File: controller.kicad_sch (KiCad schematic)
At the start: 40 parts, among them IC10 NXB0108BQX, IC11 STM32L475RGT6, IC12 W25N512GVEIG, J1 20021121-00014T4LF, J2 10118192-0001LF, Y3 ECS-.327-7-1210-TR

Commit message: Add company name (using github URL), date, and change revision number to all schematic pages
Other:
- company: (none) -> github.com/fuad1502/open-running-watch-hw
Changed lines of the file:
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@@
 	(title_block
 		(title "Open Running Watch")
-		(rev "A")
+		(date "2024-04-12")
+		(rev "0.1.0")
+		(company "github.com/fuad1502/open-running-watch-hw")
 	)
 	(junction

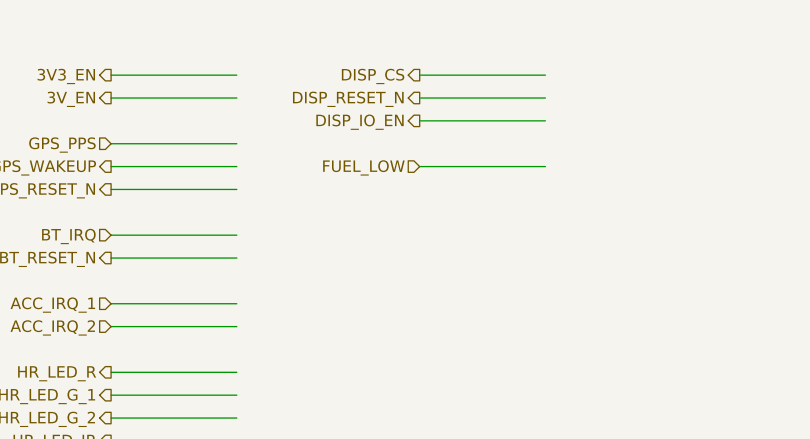
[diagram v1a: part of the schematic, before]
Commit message: Changed display to 12616-06 Sharp MIP display with Azumo backlight
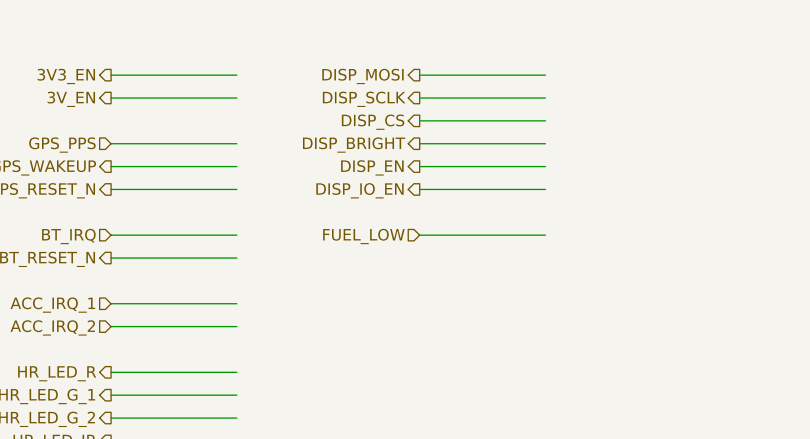
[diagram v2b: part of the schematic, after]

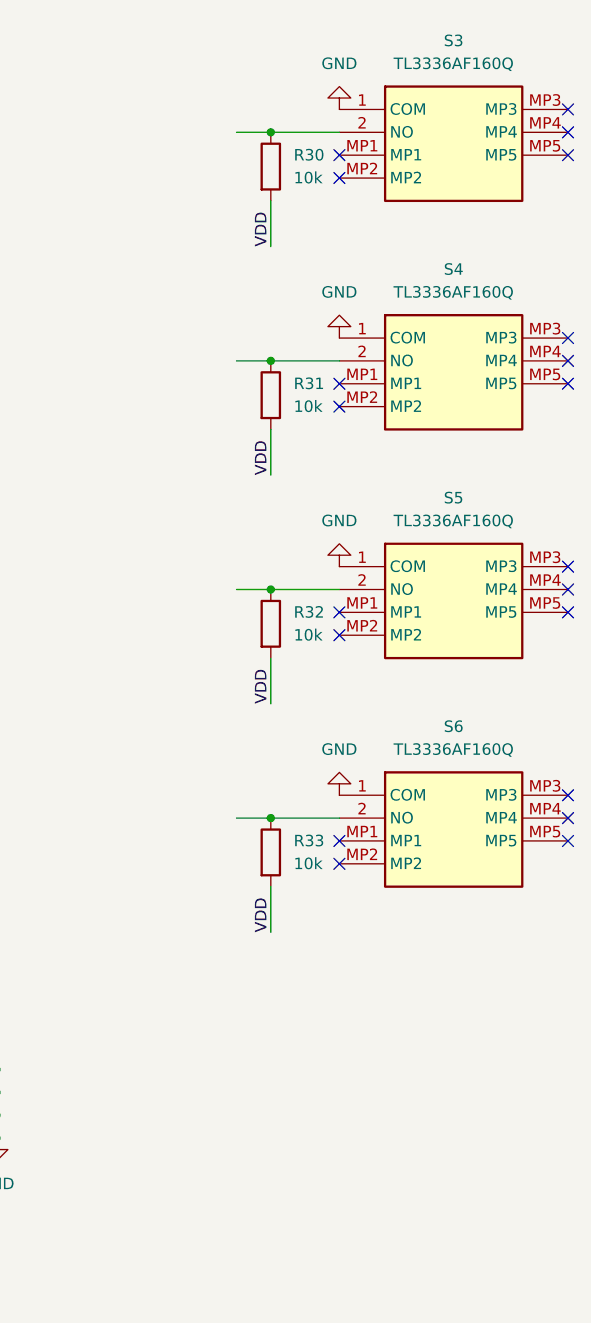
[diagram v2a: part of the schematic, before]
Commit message: Changed to smaller tactile switch
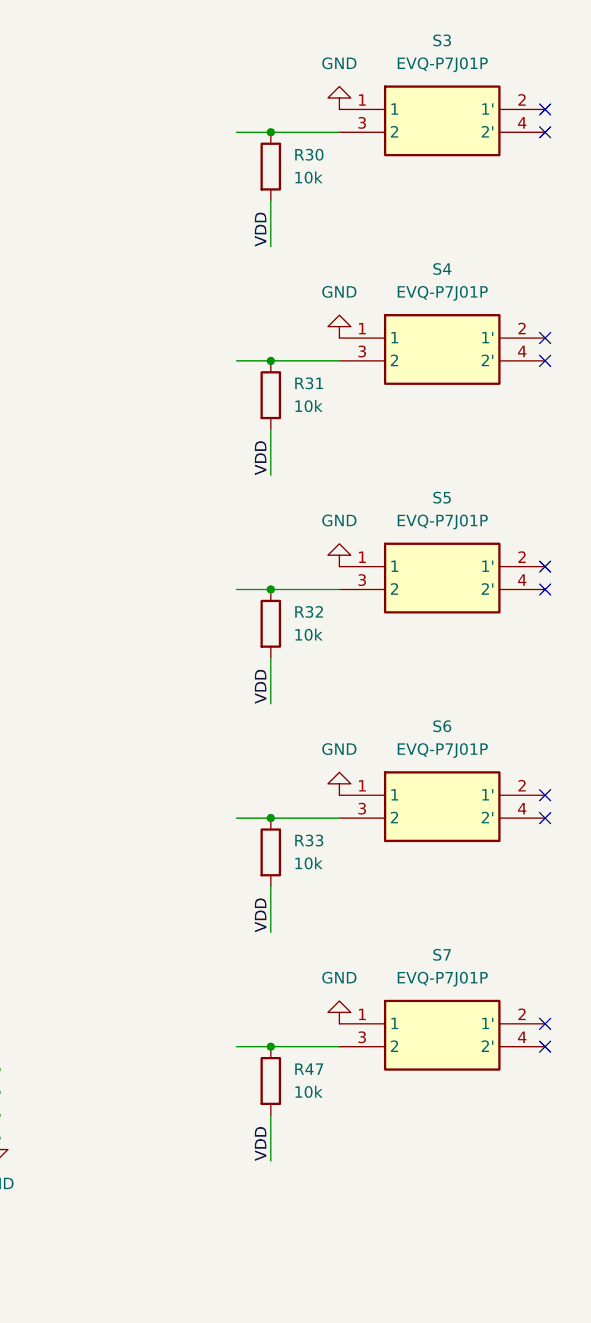
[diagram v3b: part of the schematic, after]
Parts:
- removed S3, S4, S5, S6: TL3336AF160Q, TL3336AF160Q:TL3336AF160Q, symbol TL3336AF160Q:TL3336AF160Q
- added R47: 10k, Resistor_SMD:R_0402_1005Metric_Pad0.72x0.64mm_HandSolder, symbol Device:R
- added S3, S4, S5, S6, S7: EVQ-P7J01P, EVQ-P7J01P:EVQP7J01P, symbol EVQ-P7J01P:EVQ-P7J01P
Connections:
- net GND: now also S3.1, S4.1, S5.1, S6.1, S7.1
- net VDD: now also R47.2
- net at R33.1: now also S6.3 (2)
- net at R32.1: now also S5.3 (2)
- net at R30.1: now also S3.3 (2)
- net at R31.1: now also S4.3 (2)
- new net: R47.1, S7.3 (2)
- no-connect marks 45 -> 35

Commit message: Changed hand soldered footprints to normal footprints
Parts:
- C43, C44, C45, C46, C51, C52, C53, C54, C55, C61, C62: footprint Capacitor_SMD:C_0402_1005Metric_Pad0.74x0.62mm_HandSolder -> Capacitor_SMD:C_0402_1005Metric
- C47, C48, C49, C50, C56, C57, C58, C59, C60: footprint Capacitor_SMD:C_0603_1608Metric_Pad1.08x0.95mm_HandSolder -> Capacitor_SMD:C_0603_1608Metric
- R26, R27, R28, R29, R30, R31, R32, R33, R47: footprint Resistor_SMD:R_0402_1005Metric_Pad0.72x0.64mm_HandSolder -> Resistor_SMD:R_0402_1005Metric
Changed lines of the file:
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@@
 			)
 		)
-		(property "Footprint" "Capacitor_SMD:C_0603_1608Metric_Pad1.08x0.95mm_HandSolder"
+		(property "Footprint" "Capacitor_SMD:C_0603_1608Metric"
 			(at 51.7652 231.14 0)
 			(effects
@@
 			)
 		)
-		(property "Footprint" "Capacitor_SMD:C_0402_1005Metric_Pad0.74x0.62mm_HandSolder"
+		(property "Footprint" "Capacitor_SMD:C_0402_1005Metric"
 			(at 64.4652 208.28 0)
 			(effects
@@
 			)
 		)
-		(property "Footprint" "Capacitor_SMD:C_0402_1005Metric_Pad0.74x0.62mm_HandSolder"
+		(property "Footprint" "Capacitor_SMD:C_0402_1005Metric"
 			(at 140.6652 166.37 0)
 			(effects
@@
 			)
 		)
-		(property "Footprint" "Capacitor_SMD:C_0603_1608Metric_Pad1.08x0.95mm_HandSolder"
+		(property "Footprint" "Capacitor_SMD:C_0603_1608Metric"
 			(at 77.1652 208.28 0)
 			(effects
@@
 			)
 		)
-		(property "Footprint" "Capacitor_SMD:C_0402_1005Metric_Pad0.74x0.62mm_HandSolder"
+		(property "Footprint" "Capacitor_SMD:C_0402_1005Metric"
 			(at 64.4652 182.88 0)
 			(effects
@@
 			)
 		)
-		(property "Footprint" "Capacitor_SMD:C_0603_1608Metric_Pad1.08x0.95mm_HandSolder"
+		(property "Footprint" "Capacitor_SMD:C_0603_1608Metric"
 			(at 51.7652 182.88 0)
 			(effects
@@
 			)
 		)
-		(property "Footprint" "Resistor_SMD:R_0402_1005Metric_Pad0.72x0.64mm_HandSolder"
+		(property "Footprint" "Resistor_SMD:R_0402_1005Metric"
 			(at 132.08 258.318 90)
 			(effects
@@
 			)
 		)
-		(property "Footprint" "Resistor_SMD:R_0402_1005Metric_Pad0.72x0.64mm_HandSolder"
+		(property "Footprint" "Resistor_SMD:R_0402_1005Metric"
 			(at 35.052 102.87 90)
 			(effects
@@
 			)
 		)
-		(property "Footprint" "Capacitor_SMD:C_0603_1608Metric_Pad1.08x0.95mm_HandSolder"
+		(property "Footprint" "Capacitor_SMD:C_0603_1608Metric"
 			(at 51.7652 208.28 0)
 			(effects
@@
 			)
 		)
-		(property "Footprint" "Resistor_SMD:R_0402_1005Metric_Pad0.72x0.64mm_HandSolder"
+		(property "Footprint" "Resistor_SMD:R_0402_1005Metric"
 			(at 353.822 119.38 90)
 			(effects
@@
 			)
 		)
-		(property "Footprint" "Capacitor_SMD:C_0402_1005Metric_Pad0.74x0.62mm_HandSolder"
+		(property "Footprint" "Capacitor_SMD:C_0402_1005Metric"
 			(at 39.0652 208.28 0)
 			(effects
@@
 			)
 		)
-		(property "Footprint" "Resistor_SMD:R_0402_1005Metric_Pad0.72x0.64mm_HandSolder"
+		(property "Footprint" "Resistor_SMD:R_0402_1005Metric"
 			(at 75.692 68.58 90)
 			(effects
@@
 			)
 		)
-		(property "Footprint" "Capacitor_SMD:C_0402_1005Metric_Pad0.74x0.62mm_HandSolder"
+		(property "Footprint" "Capacitor_SMD:C_0402_1005Metric"
 			(at 64.4652 254 0)
 			(effects
@@
 			)
 		)
-		(property "Footprint" "Capacitor_SMD:C_0402_1005Metric_Pad0.74x0.62mm_HandSolder"
+		(property "Footprint" "Capacitor_SMD:C_0402_1005Metric"
 			(at 39.0652 231.14 0)
 			(effects
@@
 			)
 		)
-		(property "Footprint" "Resistor_SMD:R_0402_1005Metric_Pad0.72x0.64mm_HandSolder"
+		(property "Footprint" "Resistor_SMD:R_0402_1005Metric"
 			(at 353.822 68.58 90)
 			(effects
@@
 			)
 		)
-		(property "Footprint" "Capacitor_SMD:C_0402_1005Metric_Pad0.74x0.62mm_HandSolder"
+		(property "Footprint" "Capacitor_SMD:C_0402_1005Metric"
 			(at 64.4652 231.14 0)
 			(effects
@@
 			)
 		)
-		(property "Footprint" "Resistor_SMD:R_0402_1005Metric_Pad0.72x0.64mm_HandSolder"
+		(property "Footprint" "Resistor_SMD:R_0402_1005Metric"
 			(at 353.822 43.18 90)
 			(effects
@@
 			)
 		)
-		(property "Footprint" "Capacitor_SMD:C_0402_1005Metric_Pad0.74x0.62mm_HandSolder"
+		(property "Footprint" "Capacitor_SMD:C_0402_1005Metric"
 			(at 117.8052 166.37 0)
 			(effects
@@
 			)
 		)
-		(property "Footprint" "Capacitor_SMD:C_0402_1005Metric_Pad0.74x0.62mm_HandSolder"
+		(property "Footprint" "Capacitor_SMD:C_0402_1005Metric"
 			(at 64.4652 157.48 0)
 			(effects
@@
 			)
 		)
-		(property "Footprint" "Resistor_SMD:R_0402_1005Metric_Pad0.72x0.64mm_HandSolder"
+		(property "Footprint" "Resistor_SMD:R_0402_1005Metric"
 			(at 353.822 93.98 90)
 			(effects
@@
 			)
 		)
-		(property "Footprint" "Capacitor_SMD:C_0402_1005Metric_Pad0.74x0.62mm_HandSolder"
+		(property "Footprint" "Capacitor_SMD:C_0402_1005Metric"
 			(at 39.0652 182.88 0)
 			(effects
@@
 			)
 		)
-		(property "Footprint" "Capacitor_SMD:C_0603_1608Metric_Pad1.08x0.95mm_HandSolder"
+		(property "Footprint" "Capacitor_SMD:C_0603_1608Metric"
 			(at 77.1652 231.14 0)
 			(effects
@@
 			)
 		)
-		(property "Footprint" "Capacitor_SMD:C_0603_1608Metric_Pad1.08x0.95mm_HandSolder"
+		(property "Footprint" "Capacitor_SMD:C_0603_1608Metric"
 			(at 77.1652 254 0)
 			(effects
@@
 			)
 		)
-		(property "Footprint" "Capacitor_SMD:C_0603_1608Metric_Pad1.08x0.95mm_HandSolder"
+		(property "Footprint" "Capacitor_SMD:C_0603_1608Metric"
 			(at 51.7652 157.48 0)
 			(effects
@@
 			)
 		)
-		(property "Footprint" "Capacitor_SMD:C_0402_1005Metric_Pad0.74x0.62mm_HandSolder"
+		(property "Footprint" "Capacitor_SMD:C_0402_1005Metric"
 			(at 39.0652 157.48 0)
 			(effects
@@
 			)
 		)
-		(property "Footprint" "Capacitor_SMD:C_0603_1608Metric_Pad1.08x0.95mm_HandSolder"
+		(property "Footprint" "Capacitor_SMD:C_0603_1608Metric"
 			(at 77.1652 182.88 0)
 			(effects
@@
 			)
 		)
-		(property "Footprint" "Capacitor_SMD:C_0603_1608Metric_Pad1.08x0.95mm_HandSolder"
+		(property "Footprint" "Capacitor_SMD:C_0603_1608Metric"
 			(at 77.1652 157.48 0)
 			(effects
@@
 			)
 		)
-		(property "Footprint" "Resistor_SMD:R_0402_1005Metric_Pad0.72x0.64mm_HandSolder"
+		(property "Footprint" "Resistor_SMD:R_0402_1005Metric"
 			(at 353.822 144.78 90)
 			(effects
@@
 			)
 		)
-		(property "Footprint" "Resistor_SMD:R_0402_1005Metric_Pad0.72x0.64mm_HandSolder"
+		(property "Footprint" "Resistor_SMD:R_0402_1005Metric"
 			(at 68.072 68.58 90)
 			(effects
